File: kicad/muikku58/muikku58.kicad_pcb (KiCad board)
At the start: 2 copper layers, 145.3 x 120.3 mm, 67 parts, among them J1 AudioJack4, J2 AudioJack4, SW1 RotaryEncoder_Switch, U1 RP2040_Zero

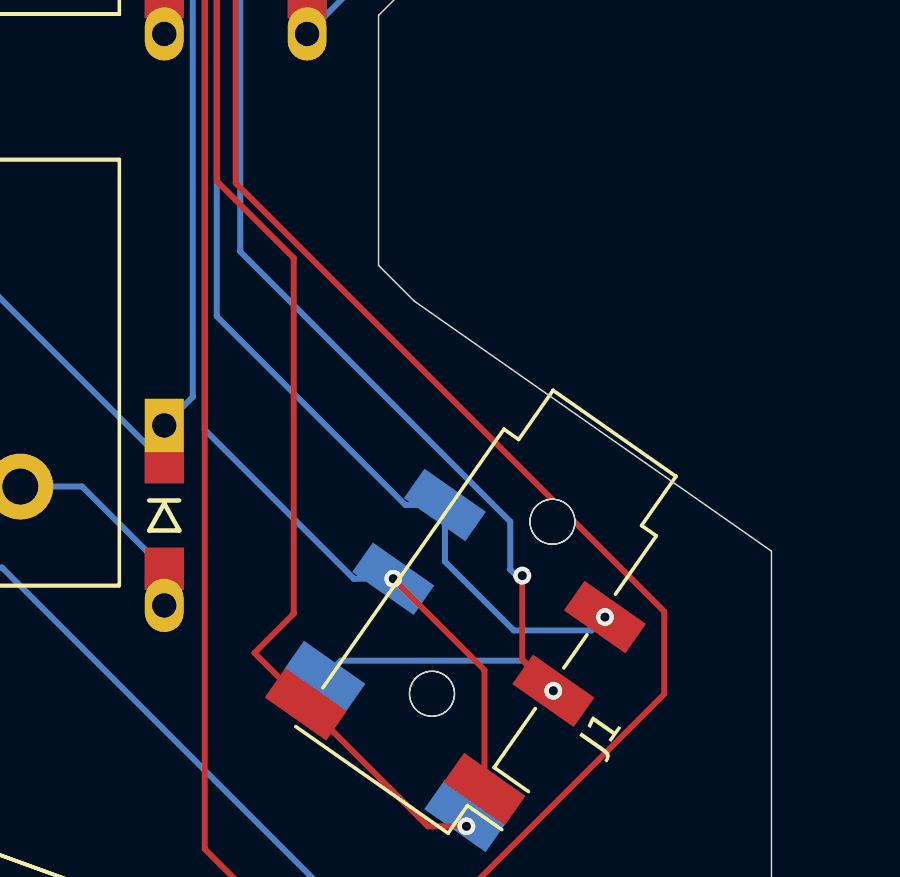
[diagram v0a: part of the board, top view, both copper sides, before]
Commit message: Fixed trace near the TRRS connector
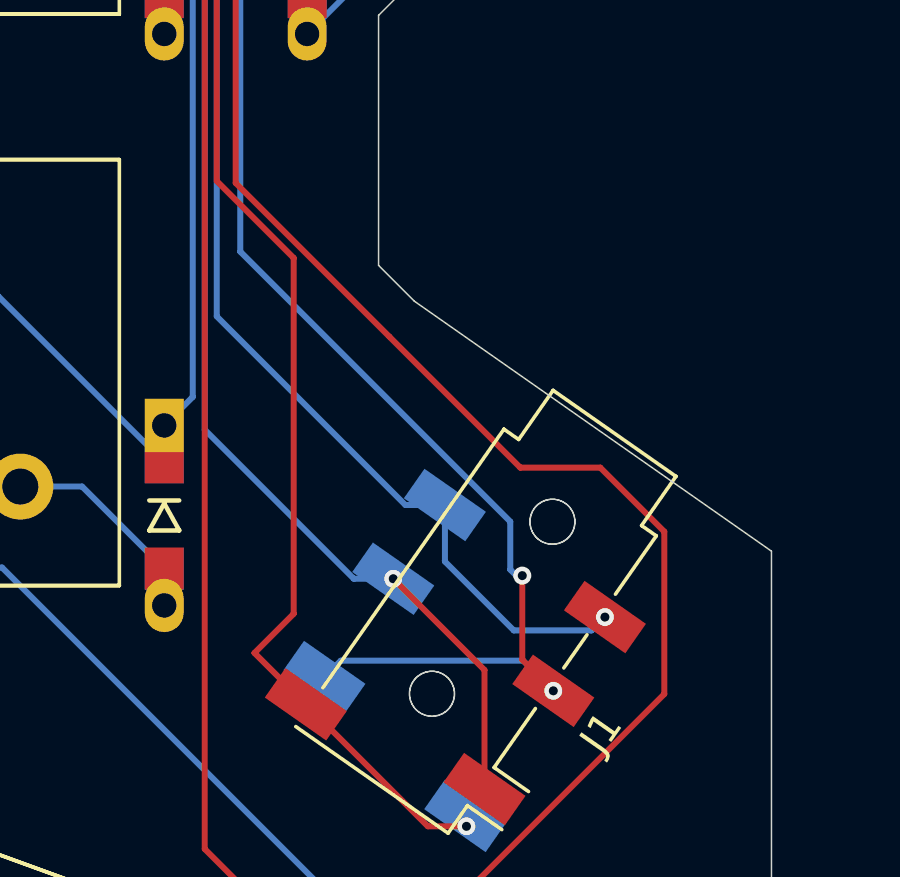
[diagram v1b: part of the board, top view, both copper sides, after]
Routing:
- net COL5: track 181.2 -> 182.8 mm
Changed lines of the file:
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@@
 	)
 	(segment
-		(start 146.446875 59.737164)
-		(end 146.446875 91.31266)
+		(start 148.511505 57.672534)
+		(end 146.446875 59.737164)
 		(width 0.2)
 		(layer "F.Cu")
@@
 	)
 	(segment
+		(start 158.6 100.8)
+		(end 160.734375 102.934375)
+		(width 0.2)
+		(layer "F.Cu")
+		(net 38)
+	)
+	(segment
+		(start 160.734375 102.934375)
+		(end 160.734375 108.346875)
+		(width 0.2)
+		(layer "F.Cu")
+		(net 38)
+	)
+	(segment
 		(start 138.1125 68.675)
 		(end 138.1125 80.881866)
@@
 		(start 138.1125 87.725)
 		(end 138.1125 98.821875)
+		(width 0.2)
+		(layer "F.Cu")
+		(net 38)
+	)
+	(segment
+		(start 146.446875 91.31266)
+		(end 151.567108 96.432892)
+		(width 0.2)
+		(layer "F.Cu")
+		(net 38)
+	)
+	(segment
+		(start 151.719409 57.672534)
+		(end 148.511505 57.672534)
 		(width 0.2)
 		(layer "F.Cu")
@@
 	)
 	(segment
-		(start 146.446875 91.31266)
-		(end 160.734375 105.60016)
-		(width 0.2)
-		(layer "F.Cu")
-		(net 38)
-	)
-	(segment
 		(start 135.46875 66.03125)
 		(end 138.1125 68.675)
@@
 	)
 	(segment
-		(start 160.734375 105.60016)
-		(end 160.734375 108.346875)
+		(start 151.567108 96.432892)
+		(end 155.934216 100.8)
 		(width 0.2)
 		(layer "F.Cu")
@@
 	)
 	(segment
-		(start 151.719409 57.672534)
-		(end 148.511505 57.672534)
+		(start 153.471875 59.425)
+		(end 151.719409 57.672534)
 		(width 0.2)
 		(layer "F.Cu")
@@
 		(start 135.46875 46.98125)
 		(end 138.1125 49.625)
+		(width 0.2)
+		(layer "F.Cu")
+		(net 38)
+	)
+	(segment
+		(start 155.934216 100.8)
+		(end 158.6 100.8)
+		(width 0.2)
+		(layer "F.Cu")
+		(net 38)
+	)
+	(segment
+		(start 146.446875 59.737164)
+		(end 146.446875 91.31266)
 		(width 0.2)
 		(layer "F.Cu")
@@
 		(width 0.2)
 		(layer "F.Cu")
-		(net 38)
-	)
-	(segment
-		(start 148.511505 57.672534)
-		(end 146.446875 59.737164)
-		(width 0.2)
-		(layer "F.Cu")
-		(net 38)
-	)
-	(segment
-		(start 153.471875 59.425)
-		(end 151.719409 57.672534)
-		(width 0.2)
-		(layer "F.Cu")

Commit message: Update muikku58.kicad_pcb
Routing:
- net TX: track 104.8 -> 105.3 mm
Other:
- board text added: "muikku58 rev 3 LEFT SIDE"
- board text removed: "muikku58 rev 2 LEFT SIDE"
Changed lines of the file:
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@@
 		)
 	)
-	(gr_text "muikku58 rev 2\n\nLEFT SIDE"
+	(gr_text "muikku58 rev 3\n\nLEFT SIDE"
 		(at 157 49.5 90)
 		(layer "F.SilkS")
@@
 	)
 	(segment
-		(start 156.028704 107.234064)
-		(end 157.034033 108.239393)
-		(width 0.2)
-		(layer "B.Cu")
-		(net 47)
-	)
-	(segment
 		(start 149.404999 107.780584)
 		(end 149.951519 107.234064)
@@
 	)
 	(segment
-		(start 149.951519 107.234064)
-		(end 156.028704 107.234064)
-		(width 0.2)
-		(layer "B.Cu")
-		(net 47)
-	)
-	(segment
 		(start 152.978156 56.6)
 		(end 146.6 62.978156)
@@
 	)
 	(segment
+		(start 149.951519 107.234064)
+		(end 150.765936 107.234064)
+		(width 0.2)
+		(layer "B.Cu")
+		(net 47)
+	)
+	(segment
+		(start 150.765936 107.234064)
+		(end 151.4 106.6)
+		(width 0.2)
+		(layer "B.Cu")
+		(net 47)
+	)
+	(segment
 		(start 166.441875 35.04189)
 		(end 166.441875 54.758125)
@@
 	)
 	(segment
+		(start 151.4 106.6)
+		(end 155.39464 106.6)
+		(width 0.2)
+		(layer "B.Cu")
+		(net 47)
+	)
+	(segment
 		(start 166.441875 54.758125)
 		(end 164.6 56.6)
 		(width 0.2)
 		(layer "B.Cu")
+		(net 47)
+	)
+	(segment
+		(start 155.39464 106.6)
+		(end 157.034033 108.239393)
+		(width 0.2)
+		(layer "B.Cu")
